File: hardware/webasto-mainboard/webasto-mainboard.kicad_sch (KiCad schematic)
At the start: 16 parts, among them J1 Console FTDI, Q1 DMG2301L, U1 CY15E004J, U2 PicoW, U3 LM4040DIM3-3.0

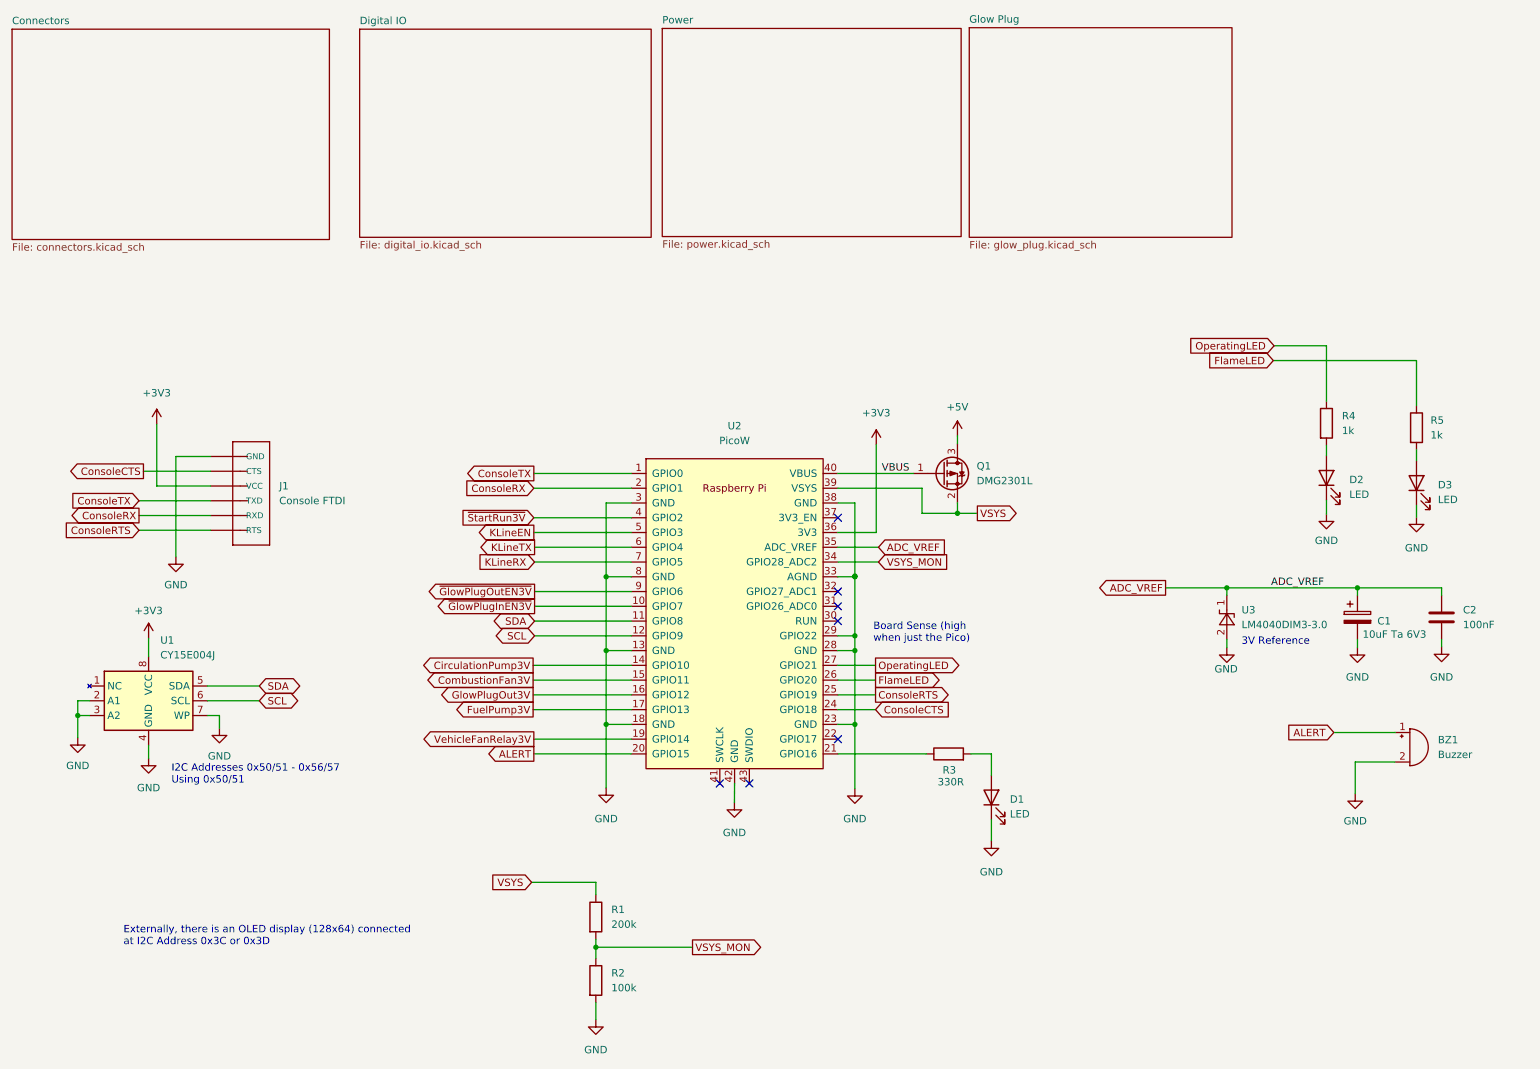
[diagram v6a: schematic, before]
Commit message: Move start/run to sensor board, add CANBUS
- WiFi is not being very helpful, and I'm concerned it won't work well once
  installed in the bus...  CANBus wiring is easy.
- Removed both Start/Run and the Vehicle Fan Relay from X1 to make space for
  canbus
- moved LEDs onto an I2C gpio extender.
- will need to still plumb in CAN_EN support
- will also need to yank out the WiFi stuff that won't stay stable anyways
  and reroute the CBOR out the CANBus instead of WiFi
- Vehicle Fan control will need to move to a LINBus fan controller board
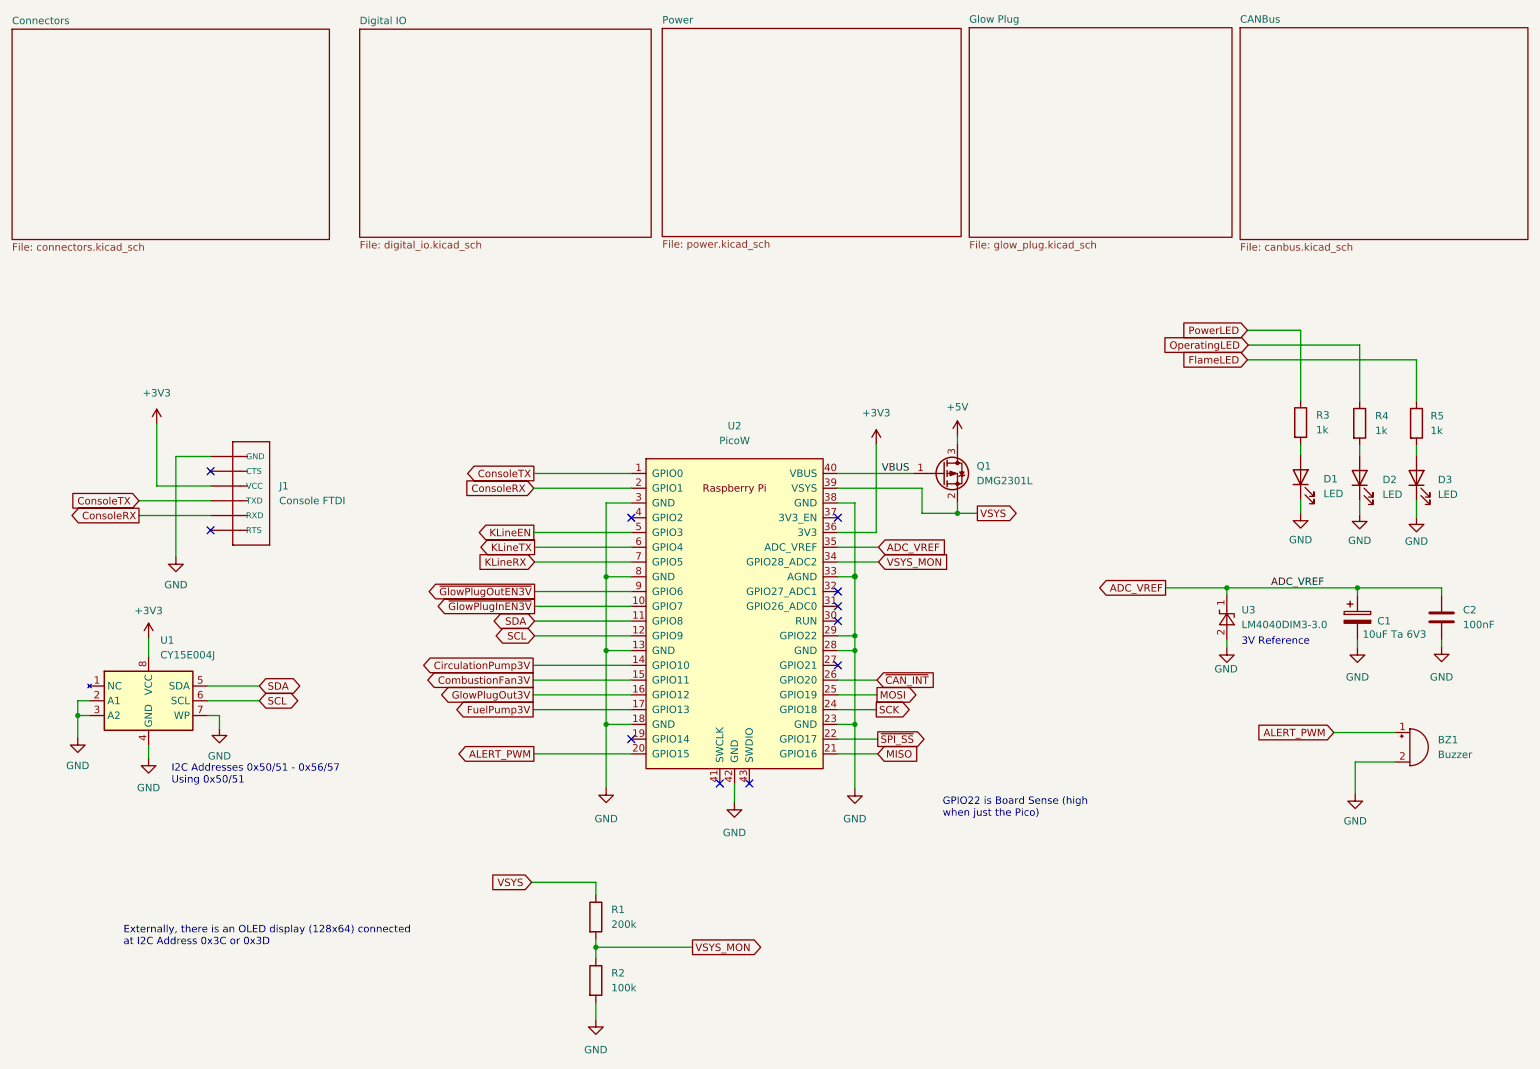
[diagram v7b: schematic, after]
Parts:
- R3: value 330R -> 1k
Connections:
- net FlameLED: no longer U2.26 (GPIO20)
- net OperatingLED: no longer U2.27 (GPIO21)
- net MISO: now reaches U2.21 (GPIO16)
- net MISO: no longer R3.1
- net ~{SPI_SS}: now reaches U2.22 (GPIO17)
- net ALERT renamed ALERT_PWM
- net ConsoleCTS: no longer names the net of J1.2 (CTS)
- net ConsoleCTS: no longer U2.24 (GPIO18)
- net ConsoleRTS: no longer names the net of J1.6 (RTS)
- net ConsoleRTS: no longer U2.25 (GPIO19)
- net VehicleFanRelay3V: no longer names the net of U2.19 (GPIO14)
- net ~{StartRun3V}: no longer names the net of U2.4 (GPIO2)
- new net MOSI: U2.25 (GPIO19)
- new net PowerLED: R3.1
- new net SCK: U2.24 (GPIO18)
- new net ~{CAN_INT}: U2.26 (GPIO20)
- no-connect marks 7 -> 11
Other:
- added sheet CANBus (canbus.kicad_sch)
- note added: "GPIO22 is Board Sense (high when just the Pico)"
- note removed: "Board Sense (high when just the Pico)"
- moved on the sheet: D2, D3, R4, R5

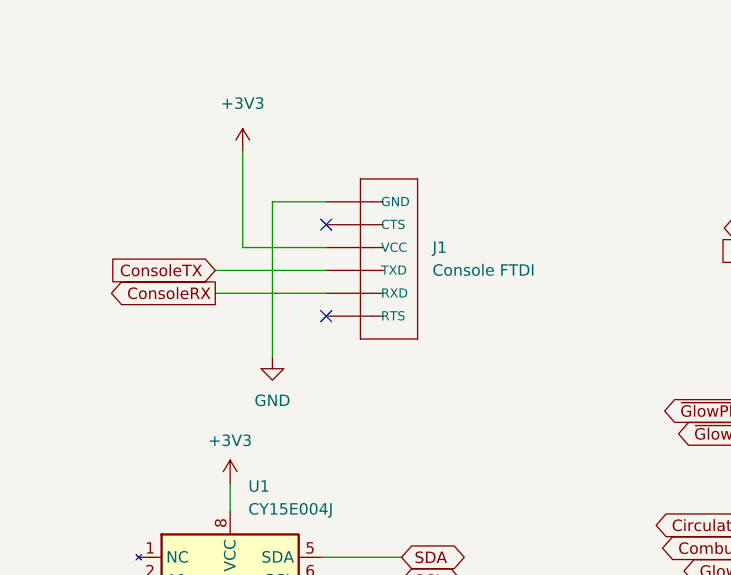
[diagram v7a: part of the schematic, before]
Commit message: Rejigger the mainboard to use voltage regulator
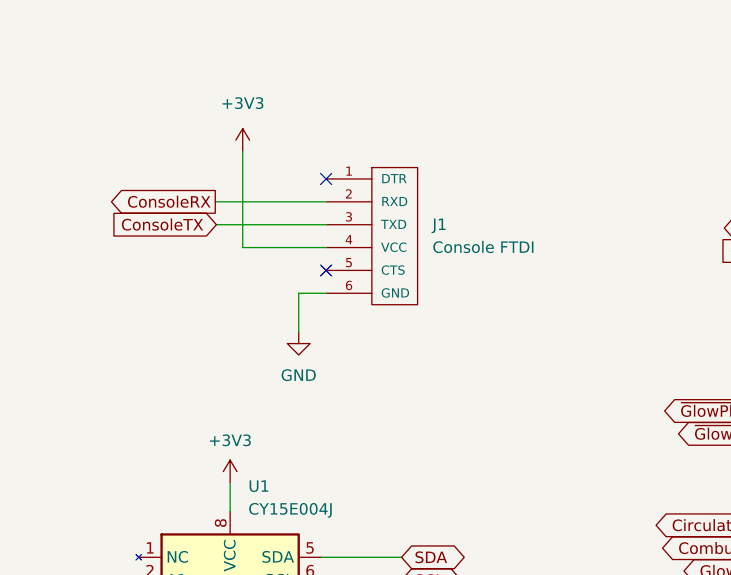
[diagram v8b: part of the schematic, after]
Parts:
- J1: footprint Beirdo:FTDI_BASIC -> Beirdo:FTDI-TARGET; symbol Beirdo:FTDI_BASICPTH -> Beirdo:FTDI-TARGET
- U2: footprint RPi_Pico:RPi_PicoW_SMD_TH -> MCU_RaspberryPi_and_Boards:RPi_Pico_SMD_TH
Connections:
- net +3V3: now also J1.4 (VCC); no longer J1.3 (VCC)
- net ConsoleRX: now also J1.2 (RXD); no longer J1.5 (RXD)
- net ConsoleTX: now also J1.3 (TXD); no longer J1.4 (TXD)
- net GND: now also J1.6 (GND); no longer J1.1 (GND)
